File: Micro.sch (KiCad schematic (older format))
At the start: 9 parts, among them J2 Conn_01x02_Male, J3 Conn_01x02_Male, J4 Conn_ARM_JTAG_SWD_10, U7 CC7V_T1A_32.768KHZ, U8 BT832

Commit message: #6 #14 - Add bluetooth and flash header to board
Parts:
- removed C23: 4.7u, symbol Device:C
- added C23: 4.7u, Capacitor_SMD:CP_Elec_4x5.3, symbol Device:CP1
- added C25: 100n, Capacitor_SMD:C_0805_2012Metric_Pad1.18x1.45mm_HandSolder, symbol Device:C
- added J5: Conn_01x08_Male, Connector_PinHeader_2.00mm:PinHeader_1x08_P2.00mm_Vertical, symbol Connector:Conn_01x08_Male
- added R13, R19: 3.3k, Resistor_SMD:R_0805_2012Metric_Pad1.20x1.40mm_HandSolder, symbol Device:R
- added R22: 10k, Resistor_SMD:R_0805_2012Metric_Pad1.20x1.40mm_HandSolder, symbol Device:R
- added R23: 1k, Resistor_SMD:R_0805_2012Metric_Pad1.20x1.40mm_HandSolder, symbol Device:R
- added TP12, TP13, TP14, TP22: TestPoint, TestPoint:TestPoint_Pad_D2.0mm, symbol Connector:TestPoint
- C15, C19, C21: footprint (none) -> Capacitor_SMD:C_0805_2012Metric_Pad1.18x1.45mm_HandSolder
- J4: footprint (none) -> Connector_PinHeader_1.27mm:PinHeader_2x05_P1.27mm_Vertical_SMD
- U8: footprint (none) -> BLE:BT832
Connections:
- net labels added: Vbatt
- wire segments 26 -> 70
- no-connect marks 0 -> 14
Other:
- note added: "Just in case a reset line is required"
- moved on the sheet: J2, J4

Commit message: #16 - Used Fanstel library
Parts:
- removed C21: 100n, Capacitor_SMD:C_0805_2012Metric_Pad1.18x1.45mm_HandSolder, symbol Device:C
- removed C23: 4.7u, Capacitor_SMD:CP_Elec_4x5.3, symbol Device:CP1
- removed J3: Conn_01x02_Male, Connector_PinHeader_2.00mm:PinHeader_1x02_P2.00mm_Vertical, symbol Connector:Conn_01x02_Male
- removed J4: Conn_ARM_JTAG_SWD_10, Connector_PinHeader_1.27mm:PinHeader_2x05_P1.27mm_Vertical_SMD, symbol Connector:Conn_ARM_JTAG_SWD_10
- removed J5: Conn_01x08_Male, Connector_PinHeader_2.00mm:PinHeader_1x08_P2.00mm_Vertical, symbol Connector:Conn_01x08_Male
- removed U8: BT832, BLE:BT832, symbol BLE:BT832
- added C21: 4.7u, Capacitor_SMD:CP_Elec_4x5.3, symbol Device:CP1
- added C23: 100n, Capacitor_SMD:C_0805_2012Metric_Pad1.18x1.45mm_HandSolder, symbol Device:C
- added J3: Conn_01x08_Male, Connector_PinHeader_2.00mm:PinHeader_1x08_P2.00mm_Vertical, symbol Connector:Conn_01x08_Male
- added J4: Conn_01x02_Male, Connector_PinHeader_2.00mm:PinHeader_1x02_P2.00mm_Vertical, symbol Connector:Conn_01x02_Male
- added J5: Conn_ARM_JTAG_SWD_10, Connector_PinHeader_1.27mm:PinHeader_2x05_P1.27mm_Vertical_SMD, symbol Connector:Conn_ARM_JTAG_SWD_10
- added U8: BT832L, Fanstel_modules:BT832-BT832L, symbol Fanstel-modules:BT832L
- R13: value 3.3k -> 1k
- R22: value 10k -> 3.3k
- R23: value 1k -> 10k
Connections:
- wire segments 70 -> 59
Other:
- note removed: "Just in case a reset line is required"

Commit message: #4 - Routed board
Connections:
- net NFC+: now reaches J2.1 (Pin_1), U8.P$7 (P09)
- net NFC-: now reaches J2.2 (Pin_2), U8.P$8 (P10)
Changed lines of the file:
@@
 	7075 3075 7075 3125
 NoConn ~ 8825 2775
+Text Label 3850 3825 0    50   ~ 0
+NFC+
+Text Label 3850 3925 0    50   ~ 0
+NFC-
 $EndSCHEMATC

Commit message: Added NFC tuning cap footprints, cleaned up silkscreen, and connected planes
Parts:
- added C26, C27: 1, Capacitor_SMD:C_0805_2012Metric_Pad1.18x1.45mm_HandSolder, symbol Device:C
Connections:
- net GND: now also C26.2, C27.2
- net NFC+: now also C27.1
- net NFC-: now also C26.1
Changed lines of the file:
@@
 $EndDescr
-$Comp
-L Fanstel-modules:BT832L U8
-U 1 1 5FE05A84
-P 5675 3575
-F 0 "U8" H 5675 4629 45  0000 C CNN
-F 1 "BT832L" H 5675 4545 45  0000 C CNN
-F 2 "Fanstel_modules:BT832-BT832L" H 5755 3725 20  0001 C CNN
-F 3 "" H 5725 3575 60  0001 C CNN
-	1    5675 3575
-	1    0    0    -1
-$EndComp
 $Comp
 L Connector:Conn_01x08_Male J3
@@
 	1    0    0    -1
 $EndComp
-Wire Wire Line
-	4525 4825 4625 4825
-Wire Wire Line
-	4625 4825 4725 4825
-Connection ~ 4625 4825
 Connection ~ 4725 4825
 Wire Wire Line
@@
 $EndComp
 Wire Wire Line
-	4275 3825 3775 3825
-Wire Wire Line
-	3775 3925 4275 3925
+	4275 3825 4150 3825
+Wire Wire Line
+	3775 3925 3825 3925
 Wire Wire Line
 	4275 3925 4275 3975
@@
 Connection ~ 3325 3525
 Wire Wire Line
-	4300 3225 4275 3225
-Wire Wire Line
 	3925 3225 3925 2950
 Wire Wire Line
@@
 Wire Wire Line
 	3075 2950 3075 3225
-Connection ~ 4275 3225
-Wire Wire Line
-	4275 3225 3925 3225
 Connection ~ 3075 3225
 Wire Wire Line
@@
 Wire Wire Line
 	4275 2650 4275 2925
-Connection ~ 4275 2925
 Wire Wire Line
 	4200 2350 4300 2350
@@
 Text Label 3850 3925 0    50   ~ 0
 NFC-
+$Comp
+L Device:C C27
+U 1 1 5FF23D29
+P 4150 4275
+F 0 "C27" H 4265 4321 50  0000 L CNN
+F 1 "1" H 4265 4230 50  0000 L CNN
+F 2 "Capacitor_SMD:C_0805_2012Metric_Pad1.18x1.45mm_HandSolder" H 4188 4125 50  0001 C CNN
+F 3 "~" H 4150 4275 50  0001 C CNN
+	1    4150 4275
+	1    0    0    -1
+$EndComp
+$Comp
+L Device:C C26
+U 1 1 5FF2493A
+P 3825 4275
+F 0 "C26" H 3940 4321 50  0000 L CNN
+F 1 "1" H 3940 4230 50  0000 L CNN
+F 2 "Capacitor_SMD:C_0805_2012Metric_Pad1.18x1.45mm_HandSolder" H 3863 4125 50  0001 C CNN
+F 3 "~" H 3825 4275 50  0001 C CNN
+	1    3825 4275
+	1    0    0    -1
+$EndComp
+Connection ~ 4275 2925
+Connection ~ 4275 3225
+Wire Wire Line
+	4275 3225 3925 3225
+Wire Wire Line
+	4300 3225 4275 3225
+Connection ~ 4625 4825
+Wire Wire Line
+	4625 4825 4725 4825
+Wire Wire Line
+	4525 4825 4625 4825
+$Comp
+L Fanstel-modules:BT832L U8
+U 1 1 5FE05A84
+P 5675 3575
+F 0 "U8" H 5675 4629 45  0000 C CNN
+F 1 "BT832L" H 5675 4545 45  0000 C CNN
+F 2 "Fanstel_modules:BT832-BT832L" H 5755 3725 20  0001 C CNN
+F 3 "" H 5725 3575 60  0001 C CNN
+	1    5675 3575
+	1    0    0    -1
+$EndComp
+Wire Wire Line
+	3825 3925 3825 4125
+Connection ~ 3825 3925
+Wire Wire Line
+	3825 3925 4275 3925
+Wire Wire Line
+	4150 4125 4150 3825
+Connection ~ 4150 3825
+Wire Wire Line
+	4150 3825 3775 3825
+Wire Wire Line
+	3825 4425 3975 4425
+Wire Wire Line
+	3975 4425 3975 4825
+Wire Wire Line
+	3975 4825 4525 4825
+Connection ~ 3975 4425
+Wire Wire Line
+	3975 4425 4150 4425
+Connection ~ 4525 4825
 $EndSCHEMATC

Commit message: #19 and #20 - Fix the micro debug and power connections
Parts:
- added R24, R25: 100k, Resistor_SMD:R_0805_2012Metric_Pad1.20x1.40mm_HandSolder, symbol Device:R
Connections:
- net 3.3V: now also C21.1, C23.1, U8.P$9 (VDD), R24.1
- net GND: now also C21.2, C23.2, U8.P$10 (GND), R25.2
- net at J5.4 (SWDCLK/TCK), U8.P$15 (SWCLK): now also R25.1
- net at J5.2 (SWDIO/TMS), U8.P$16 (SWDIO): now also R24.2
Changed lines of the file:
@@
 U 1 1 5FF492F1
 P 8825 3275
-F 0 "TP22" V 8775 3325 50  0000 C CNN
-F 1 "TestPoint" V 8825 3650 50  0000 C CNN
+F 0 "TP22" V 8725 3400 50  0000 C CNN
+F 1 "TestPoint" V 8900 3500 50  0000 C CNN
 F 2 "TestPoint:TestPoint_Pad_D2.0mm" H 9025 3275 50  0001 C CNN
 F 3 "~" H 9025 3275 50  0001 C CNN
@@
 $EndComp
 Wire Wire Line
-	8825 2975 7075 2975
+	8825 2975 8150 2975
 Wire Wire Line
-	8825 3075 7075 3075
+	8825 3075 8250 3075
 Wire Wire Line
 	7075 3075 7075 3125
@@
 	3975 4425 4150 4425
 Connection ~ 4525 4825
+$Comp
+L Device:R R24
+U 1 1 601D1E80
+P 8150 2825
+F 0 "R24" H 8220 2871 50  0000 L CNN
+F 1 "100k" H 8220 2780 50  0000 L CNN
+F 2 "Resistor_SMD:R_0805_2012Metric_Pad1.20x1.40mm_HandSolder" V 8080 2825 50  0001 C CNN
+F 3 "~" H 8150 2825 50  0001 C CNN
+	1    8150 2825
+	1    0    0    -1
+$EndComp
+Connection ~ 8150 2975
+Wire Wire Line
+	8150 2975 7075 2975
+Text GLabel 8150 2675 1    50   Input ~ 0
+3.3V
+$Comp
+L Device:R R25
+U 1 1 601D40AD
+P 8250 3225
+F 0 "R25" H 8050 3275 50  0000 L CNN
+F 1 "100k" H 8000 3175 50  0000 L CNN
+F 2 "Resistor_SMD:R_0805_2012Metric_Pad1.20x1.40mm_HandSolder" V 8180 3225 50  0001 C CNN
+F 3 "~" H 8250 3225 50  0001 C CNN
+	1    8250 3225
+	1    0    0    -1
+$EndComp
+Connection ~ 8250 3075
+Wire Wire Line
+	8250 3075 7075 3075
+$Comp
+L power:GND #PWR022
+U 1 1 601D52B6
+P 8250 3375
+F 0 "#PWR022" H 8250 3125 50  0001 C CNN
+F 1 "GND" H 8325 3250 50  0000 C CNN
+F 2 "" H 8250 3375 50  0001 C CNN
+F 3 "" H 8250 3375 50  0001 C CNN
+	1    8250 3375
+	1    0    0    -1
+$EndComp
+Text GLabel 7700 4175 2    50   Input ~ 0
+3.3V
+$Comp
+L power:GND #PWR0101
+U 1 1 601E3062
+P 8150 3875
+F 0 "#PWR0101" H 8150 3625 50  0001 C CNN
+F 1 "GND" H 8225 3750 50  0000 C CNN
+F 2 "" H 8150 3875 50  0001 C CNN
+F 3 "" H 8150 3875 50  0001 C CNN
+	1    8150 3875
+	1    0    0    -1
+$EndComp
+Wire Wire Line
+	8150 3875 7700 3875
+Connection ~ 7700 3875
 $EndSCHEMATC

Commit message: #22 - Detach battery ADC while the micro is not powered
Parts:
- removed TP14, TP22: TestPoint, TestPoint:TestPoint_Pad_D2.0mm, symbol Connector:TestPoint
- added Q2: Q_NMOS_DGS, Package_TO_SOT_SMD:TSOT-23, symbol Device:Q_NMOS_DGS
- added R27: 100, Resistor_SMD:R_0805_2012Metric_Pad1.20x1.40mm_HandSolder, symbol Device:R
- added R28: 2k, Resistor_SMD:R_0805_2012Metric_Pad1.20x1.40mm_HandSolder, symbol Device:R
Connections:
- net 3.3V: now also R27.2
- net GND: now also R28.1
- net Vbatt: now also Q2.1 (D); no longer R13.2
- net at U8.P$14 (P21/RESET): now also R28.2
- new net: Q2.3 (S), R13.2
- new net: Q2.2 (G), R27.1
- no-connect marks 14 -> 15
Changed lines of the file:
@@
 	0    1    1    0
 $EndComp
-Text GLabel 3775 3675 0    50   Input ~ 0
+Text GLabel 2200 3325 1    50   Input ~ 0
 Vbatt
 Wire Wire Line
@@
 Text GLabel 7925 3425 2    50   Input ~ 0
 3.3V
-$Comp
-L Connector:TestPoint TP14
-U 1 1 5FF3BCE7
-P 7075 3275
-F 0 "TP14" V 7025 3325 50  0000 C CNN
-F 1 "TestPoint" V 7075 3650 50  0000 C CNN
-F 2 "TestPoint:TestPoint_Pad_D2.0mm" H 7275 3275 50  0001 C CNN
-F 3 "~" H 7275 3275 50  0001 C CNN
-	1    7075 3275
-	0    1    1    0
-$EndComp
 NoConn ~ 8825 2875
 Connection ~ 9325 2375
@@
 	1    9325 2375
 	-1   0    0    1
-$EndComp
-$Comp
-L Connector:TestPoint TP22
-U 1 1 5FF492F1
-P 8825 3275
-F 0 "TP22" V 8725 3400 50  0000 C CNN
-F 1 "TestPoint" V 8900 3500 50  0000 C CNN
-F 2 "TestPoint:TestPoint_Pad_D2.0mm" H 9025 3275 50  0001 C CNN
-F 3 "~" H 9025 3275 50  0001 C CNN
-	1    8825 3275
-	0    -1   -1   0
 $EndComp
 Text GLabel 9325 3575 3    50   Input ~ 0
@@
 	8150 3875 7700 3875
 Connection ~ 7700 3875
+NoConn ~ 8825 3275
+$Comp
+L Device:Q_NMOS_DGS Q2
+U 1 1 60201D44
+P 2100 3525
+F 0 "Q2" H 2304 3571 50  0000 L CNN
+F 1 "Q_NMOS_DGS" H 2304 3480 50  0000 L CNN
+F 2 "Package_TO_SOT_SMD:TSOT-23" H 2300 3625 50  0001 C CNN
+F 3 "~" H 2100 3525 50  0001 C CNN
+	1    2100 3525
+	1    0    0    -1
+$EndComp
+$Comp
+L Device:R R27
+U 1 1 60208692
+P 1750 3525
+F 0 "R27" V 1543 3525 50  0000 C CNN
+F 1 "100" V 1634 3525 50  0000 C CNN
+F 2 "Resistor_SMD:R_0805_2012Metric_Pad1.20x1.40mm_HandSolder" V 1680 3525 50  0001 C CNN
+F 3 "~" H 1750 3525 50  0001 C CNN
+	1    1750 3525
+	0    1    1    0
+$EndComp
+Wire Wire Line
+	3775 3725 3775 3675
+Wire Wire Line
+	2200 3725 3775 3725
+Text GLabel 1600 3525 0    50   Input ~ 0
+3.3V
+$Comp
+L Device:R R28
+U 1 1 60220F36
+P 7225 3275
+F 0 "R28" V 7100 3425 50  0000 C CNN
+F 1 "2k" V 7109 3275 50  0000 C CNN
+F 2 "Resistor_SMD:R_0805_2012Metric_Pad1.20x1.40mm_HandSolder" V 7155 3275 50  0001 C CNN
+F 3 "~" H 7225 3275 50  0001 C CNN
+	1    7225 3275
+	0    1    1    0
+$EndComp
+$Comp
+L power:GND #PWR024
+U 1 1 602219D1
+P 7375 3275
+F 0 "#PWR024" H 7375 3025 50  0001 C CNN
+F 1 "GND" H 7450 3150 50  0000 C CNN
+F 2 "" H 7375 3275 50  0001 C CNN
+F 3 "" H 7375 3275 50  0001 C CNN
+	1    7375 3275
+	1    0    0    -1
+$EndComp
 $EndSCHEMATC

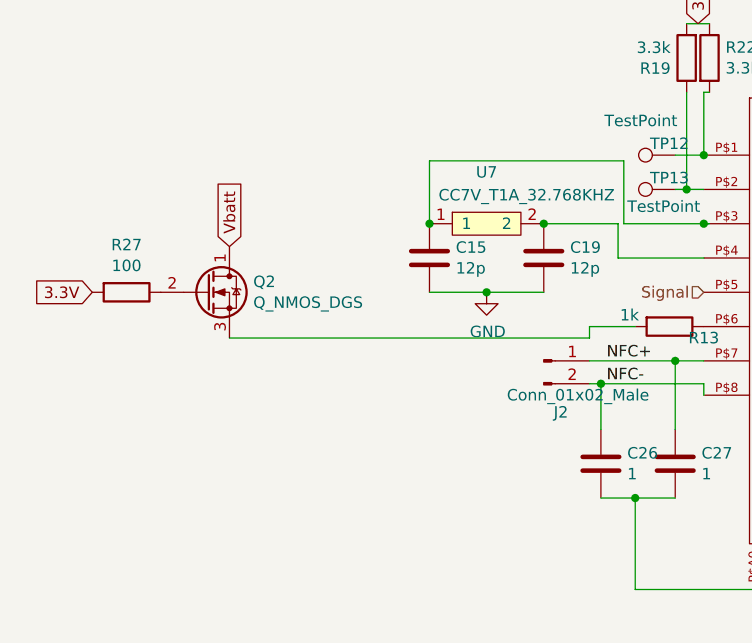
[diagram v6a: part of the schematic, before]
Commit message: #23 - Add high side power switcher
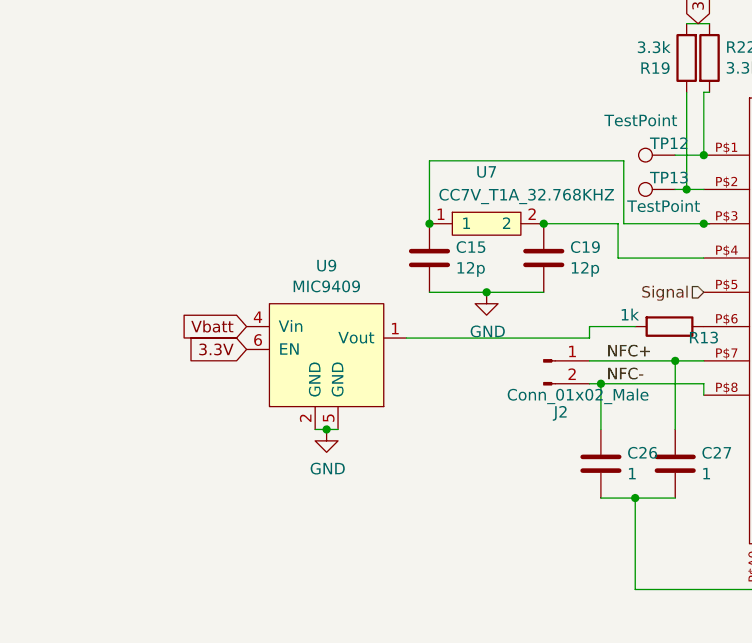
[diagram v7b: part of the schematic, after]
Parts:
- removed Q2: Q_NMOS_DGS, Package_TO_SOT_SMD:TSOT-23, symbol Device:Q_NMOS_DGS
- removed R27: 100, Resistor_SMD:R_0805_2012Metric_Pad1.20x1.40mm_HandSolder, symbol Device:R
- added U9: MIC9409, Package_TO_SOT_SMD:SOT-363_SC-70-6_Handsoldering, symbol Switches:MIC9409
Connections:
- net 3.3V: now also U9.6 (EN)
- net GND: now also U9.2 (GND), U9.5 (GND)
- net Vbatt: now also U9.4 (Vin)
- net at R13.2: now also U9.1 (Vout)
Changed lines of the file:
@@
 	0    1    1    0
 $EndComp
-Text GLabel 2200 3325 1    50   Input ~ 0
-Vbatt
 Wire Wire Line
 	3975 3675 3775 3675
@@
 $EndComp
 $Comp
-L Device:C C15
-U 1 1 5FEA0A42
-P 3075 3375
-F 0 "C15" H 3190 3421 50  0000 L CNN
-F 1 "12p" H 3190 3330 50  0000 L CNN
-F 2 "Capacitor_SMD:C_0805_2012Metric_Pad1.18x1.45mm_HandSolder" H 3113 3225 50  0001 C CNN
-F 3 "~" H 3075 3375 50  0001 C CNN
-	1    3075 3375
-	1    0    0    -1
-$EndComp
-$Comp
 L power:GND #PWR015
 U 1 1 5FEA1864
@@
 $EndComp
 Wire Wire Line
-	3075 3525 3325 3525
-Wire Wire Line
 	3575 3525 3325 3525
-Connection ~ 3325 3525
 Wire Wire Line
 	3925 3225 3925 2950
 Wire Wire Line
 	3925 2950 3075 2950
-Wire Wire Line
-	3075 2950 3075 3225
-Connection ~ 3075 3225
 Wire Wire Line
 	3575 3225 3900 3225
@@
 Connection ~ 7700 3875
 NoConn ~ 8825 3275
-$Comp
-L Device:Q_NMOS_DGS Q2
-U 1 1 60201D44
-P 2100 3525
-F 0 "Q2" H 2304 3571 50  0000 L CNN
-F 1 "Q_NMOS_DGS" H 2304 3480 50  0000 L CNN
-F 2 "Package_TO_SOT_SMD:TSOT-23" H 2300 3625 50  0001 C CNN
-F 3 "~" H 2100 3525 50  0001 C CNN
-	1    2100 3525
-	1    0    0    -1
-$EndComp
-$Comp
-L Device:R R27
-U 1 1 60208692
-P 1750 3525
-F 0 "R27" V 1543 3525 50  0000 C CNN
-F 1 "100" V 1634 3525 50  0000 C CNN
-F 2 "Resistor_SMD:R_0805_2012Metric_Pad1.20x1.40mm_HandSolder" V 1680 3525 50  0001 C CNN
-F 3 "~" H 1750 3525 50  0001 C CNN
-	1    1750 3525
-	0    1    1    0
-$EndComp
 Wire Wire Line
 	3775 3725 3775 3675
-Wire Wire Line
-	2200 3725 3775 3725
-Text GLabel 1600 3525 0    50   Input ~ 0
-3.3V
 $Comp
 L Device:R R28
@@
 	1    0    0    -1
 $EndComp
+Connection ~ 3075 3225
+Connection ~ 3325 3525
+Wire Wire Line
+	3075 2950 3075 3225
+Wire Wire Line
+	2625 4125 2675 4125
+Connection ~ 2625 4125
+$Comp
+L power:GND #PWR026
+U 1 1 6035D78D
+P 2625 4125
+F 0 "#PWR026" H 2625 3875 50  0001 C CNN
+F 1 "GND" H 2630 3952 50  0000 C CNN
+F 2 "" H 2625 4125 50  0001 C CNN
+F 3 "" H 2625 4125 50  0001 C CNN
+	1    2625 4125
+	1    0    0    -1
+$EndComp
+Wire Wire Line
+	2575 4125 2625 4125
+$Comp
+L Switches:MIC9409 U9
+U 1 1 6035A63D
+P 2575 3675
+F 0 "U9" H 2625 3940 50  0000 C CNN
+F 1 "MIC9409" H 2625 3849 50  0000 C CNN
+F 2 "Package_TO_SOT_SMD:SOT-363_SC-70-6_Handsoldering" H 2575 3675 50  0001 C CNN
+F 3 "https://ww1.microchip.com/downloads/en/DeviceDoc/mic9409x.pdf" H 2575 3675 50  0001 C CNN
+	1    2575 3675
+	1    0    0    -1
+$EndComp
+Text GLabel 2275 3775 0    50   Input ~ 0
+3.3V
+Wire Wire Line
+	3075 3525 3325 3525
+$Comp
+L Device:C C15
+U 1 1 5FEA0A42
+P 3075 3375
+F 0 "C15" H 3190 3421 50  0000 L CNN
+F 1 "12p" H 3190 3330 50  0000 L CNN
+F 2 "Capacitor_SMD:C_0805_2012Metric_Pad1.18x1.45mm_HandSolder" H 3113 3225 50  0001 C CNN
+F 3 "~" H 3075 3375 50  0001 C CNN
+	1    3075 3375
+	1    0    0    -1
+$EndComp
+Text GLabel 2275 3675 0    50   Input ~ 0
+Vbatt
+Wire Wire Line
+	3775 3725 2975 3725
 $EndSCHEMATC

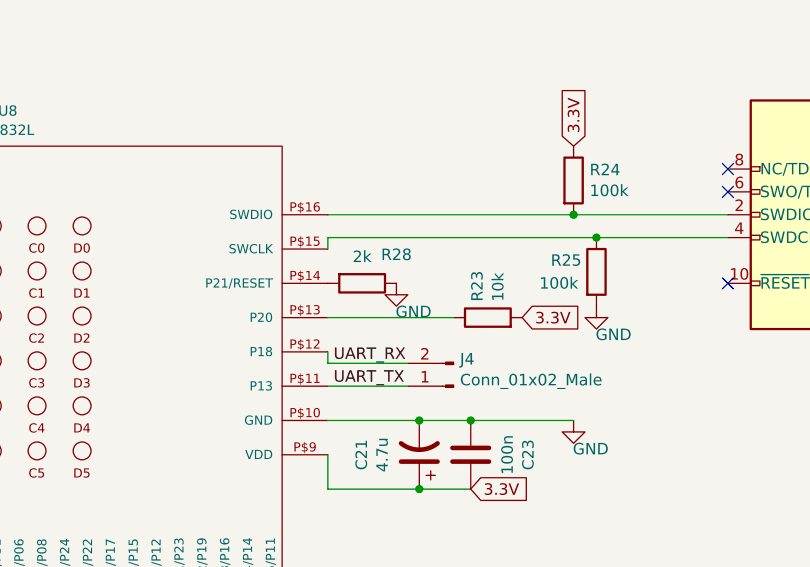
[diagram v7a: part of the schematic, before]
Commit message: Added mounting holes, Added lead-detect to a micro GPIO, and removed requirement that the leads must be attached prior to turning on the device
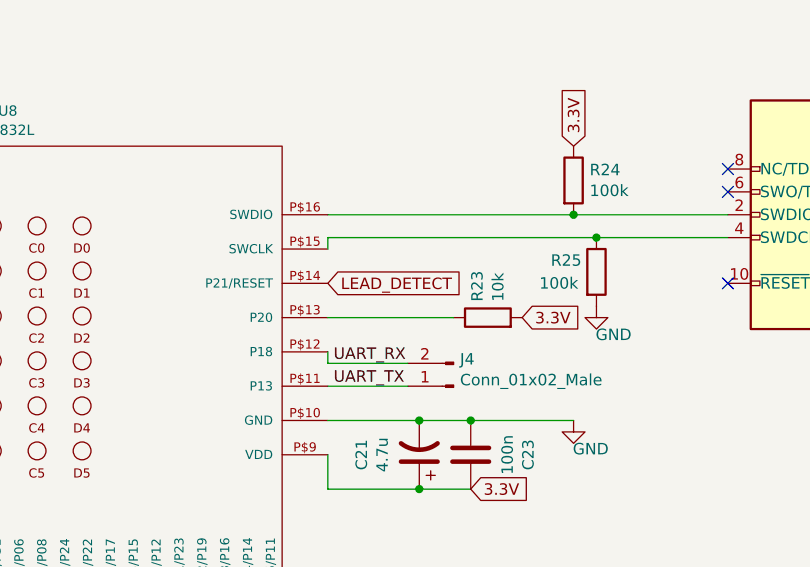
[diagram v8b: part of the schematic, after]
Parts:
- removed R28: 2k, Resistor_SMD:R_0805_2012Metric_Pad1.20x1.40mm_HandSolder, symbol Device:R
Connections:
- net LEAD_DETECT: now reaches U8.P$14 (P21/RESET)
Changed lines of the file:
@@
 Wire Wire Line
 	3775 3725 3775 3675
-$Comp
-L Device:R R28
-U 1 1 60220F36
-P 7225 3275
-F 0 "R28" V 7100 3425 50  0000 C CNN
-F 1 "2k" V 7109 3275 50  0000 C CNN
-F 2 "Resistor_SMD:R_0805_2012Metric_Pad1.20x1.40mm_HandSolder" V 7155 3275 50  0001 C CNN
-F 3 "~" H 7225 3275 50  0001 C CNN
-	1    7225 3275
-	0    1    1    0
-$EndComp
-$Comp
-L power:GND #PWR024
-U 1 1 602219D1
-P 7375 3275
-F 0 "#PWR024" H 7375 3025 50  0001 C CNN
-F 1 "GND" H 7450 3150 50  0000 C CNN
-F 2 "" H 7375 3275 50  0001 C CNN
-F 3 "" H 7375 3275 50  0001 C CNN
-	1    7375 3275
-	1    0    0    -1
-$EndComp
 Connection ~ 3075 3225
 Connection ~ 3325 3525
@@
 Wire Wire Line
 	3775 3725 2975 3725
+Text GLabel 7075 3275 2    50   Input ~ 0
+LEAD_DETECT
 $EndSCHEMATC
